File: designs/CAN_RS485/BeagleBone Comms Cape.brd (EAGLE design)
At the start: 71.8 x 58.4 mm, 59 parts, among them T1 PBSS4350Z 50V 3A, T2 PBSS4350Z 50V 3A, T3 PBSS4350Z 50V 3A, T4 PBSS4350Z 50V 3A, T5 PBSS4350Z 50V 3A, T6 PBSS4350Z 50V 3A, T7 PBSS4350Z 50V 3A, T8 PBSS4350Z 50V 3A

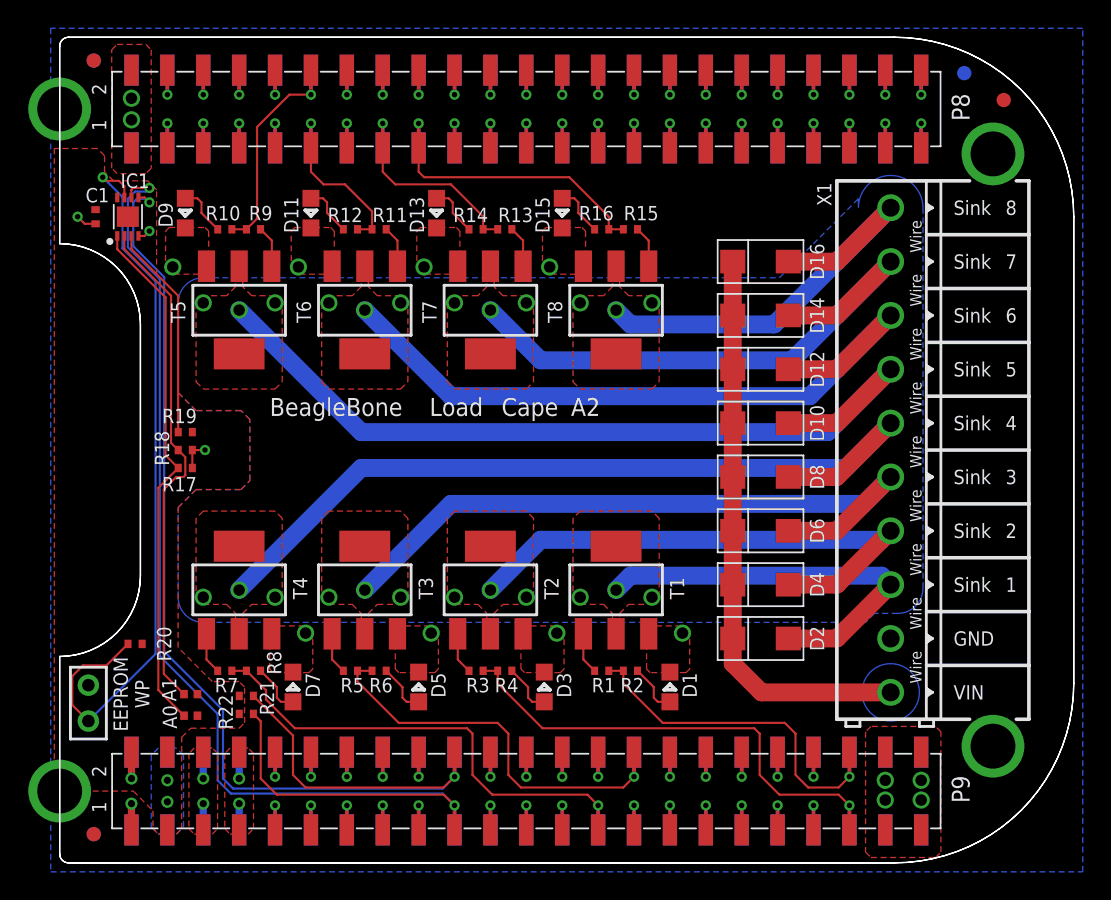
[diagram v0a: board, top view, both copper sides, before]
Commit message: Added the revised EAGLE schematics. Also removed two files that were probably not intended to be added as they are lock files in EAGLE.
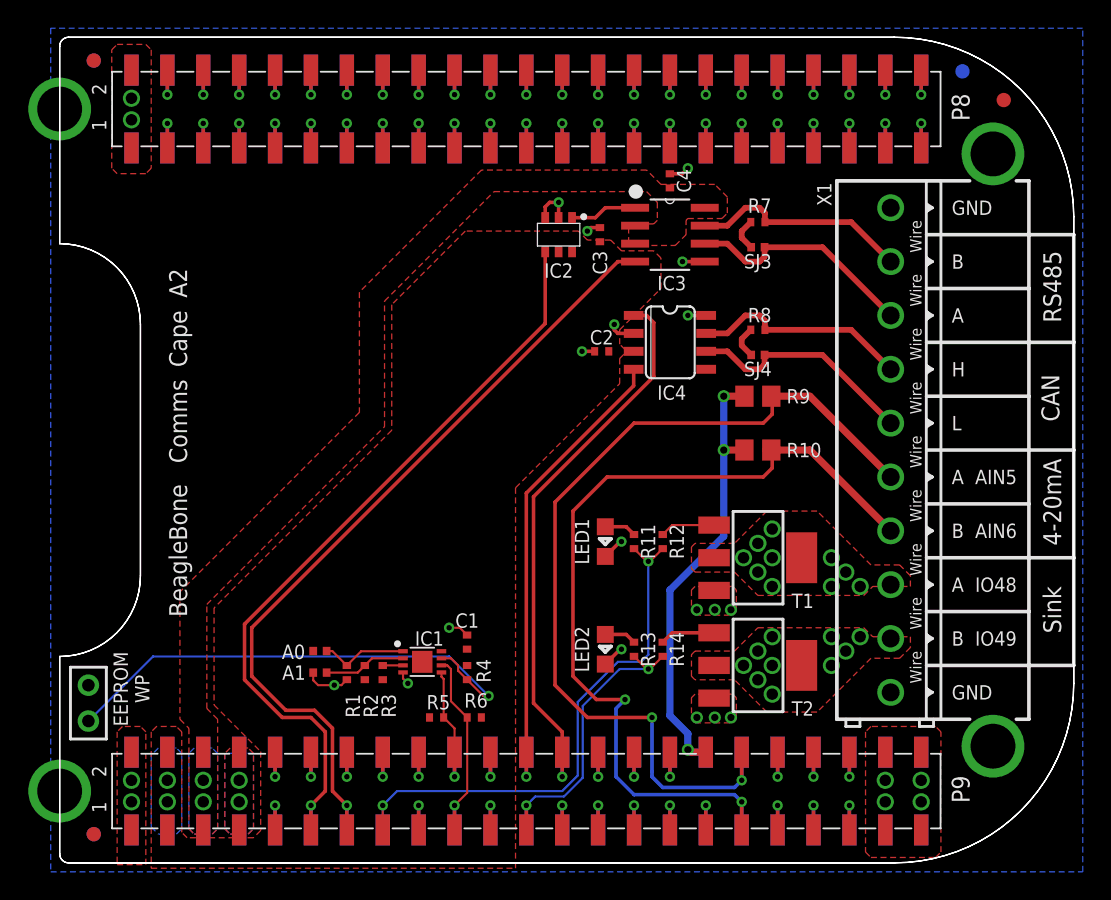
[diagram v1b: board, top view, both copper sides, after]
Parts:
- removed D1, D11, D13, D15, D3, D5, D7, D9: RED, GHI-BasicComponents:0805-LED
- removed D10, D12, D14, D16, D2, D4, D6, D8: STPS140A, GHI:DIODE_SMA
- removed R15: 330, GHI-BasicComponents:0402
- removed R16, R17, R18, R19, R20: 1k, GHI-BasicComponents:0402
- removed R21, R22: DNP(2.2k), GHI-BasicComponents:0402
- removed T3, T4, T5, T6, T7, T8: PBSS4350Z 50V 3A, GHI-Transistors:SOT223
- added C2, C3, C4: .1uF, GHI-BasicComponents:0402
- added IC2: 74LVC1G57, GHI2:SOT-23-6
- added IC3: MAX13487EESA, GHI3:SOIC8
- added IC4: SN65HVD230, GHI:SO8
- added LED1, LED2: (no value), GHI-BasicComponents:0805-LED
- added SJ3, SJ4: (no value), GHI-Miscellaneous:SOLDER.JOINT(0402)
- C1: value (none) -> .1uF
- R1, R11, R13, R3: value 330 -> 1k
- R10: value 1k -> 75 .125W; device GHI-BasicComponents:0402 -> GHI-BasicComponents:0805
- R12, R14: value 1k -> 330
- R5: value 330 -> DNP(2.2k)
- R6: value 1k -> DNP(2.2k)
- R7: value 330 -> 120
- R8: value 1k -> 120
- R9: value 330 -> 75 .125W; device GHI-BasicComponents:0402 -> GHI-BasicComponents:0805
- moved R7 49.3 mm to (49.4, 45.3), turned to 0 degrees
- moved R8 43.1 mm to (49.4, 37.7)
- moved R10 40.8 mm to (49.4, 29.2), turned to 0 degrees
- moved C1 40.0 mm to (28.8, 15.6), turned to 90 degrees
- moved IC1 37.8 mm to (25.7, 14.2), turned to 90 degrees
- moved R9 37.6 mm to (49.4, 33.0)
- moved R14 32.5 mm to (42.7, 15.1), turned to 90 degrees
- moved R12 31.3 mm to (42.7, 22.7), turned to 90 degrees
- moved R13 31.1 mm to (40.6, 15.1), turned to 90 degrees
- moved R11 28.5 mm to (40.6, 22.7), turned to 90 degrees
- moved T2 19.7 mm to (49.4, 14.0), turned to 270 degrees
- moved R2 18.8 mm to (21.6, 13.5), turned to 90 degrees
- moved R1 18.0 mm to (20.3, 13.5), turned to 90 degrees
- moved T1 10.3 mm to (49.4, 21.6), turned to 270 degrees
- moved SJ1 10.2 mm to (18.4, 15.0), turned to 0 degrees
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- renumbered BB.CAPE1 to BB.CAPE2
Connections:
- removed net N$10: R7.2, T4.1
- removed net N$11: D5.A, R6.2
- removed net N$12: R5.2, T3.1
- removed net N$13: D3.A, R4.2
- removed net N$3: D13.A, R14.2
- removed net N$35: R3.2, T2.1
- removed net N$36: D1.A, R2.2
- removed net N$37: R1.2, T1.1
- removed net N$38: D15.A, R16.2
- removed net N$39: R15.2, T8.1
- removed net N$6: R11.2, T6.1
- removed net N$9: D7.A, R8.2
- removed net P9.11: BB.CAPE2.B9.11, BB.CAPE2.T9.11
- removed net P9.13: BB.CAPE2.B9.13, BB.CAPE2.T9.13
- removed net P9.15: BB.CAPE2.B9.15, BB.CAPE2.T9.15
- removed net P9.23: BB.CAPE2.B9.23, BB.CAPE2.T9.23
- removed net P9.24: BB.CAPE2.B9.24, BB.CAPE2.T9.24
- removed net P9.26: BB.CAPE2.B9.26, BB.CAPE2.T9.26
- removed net P9.34: BB.CAPE2.B9.34, BB.CAPE2.T9.34
- removed net P9.35: BB.CAPE2.B9.35, BB.CAPE2.T9.35
- removed net P9.36: BB.CAPE2.B9.36, BB.CAPE2.T9.36
- removed net SINK1: BB.CAPE2.B9.42, BB.CAPE2.T9.42, R1.1, R2.1
- removed net SINK1.TB: D2.A, T1.2, T1.4, X1.8
- removed net SINK2: BB.CAPE2.B9.41, BB.CAPE2.T9.41, R3.1, R4.1
- removed net SINK2.TB: D4.A, T2.2, T2.4, X1.7
- removed net SINK3: BB.CAPE2.B9.30, BB.CAPE2.T9.30, R5.1, R6.1
- removed net SINK3.TB: D6.A, T3.2, T3.4, X1.6
- removed net SINK4: BB.CAPE2.B9.27, BB.CAPE2.T9.27, R7.1, R8.1
- removed net SINK4.TB: D8.A, T4.2, T4.4, X1.5
- removed net SINK5: BB.CAPE2.B8.12, BB.CAPE2.T8.12, R10.1, R9.1
- removed net SINK5.TB: D10.A, T5.2, T5.4, X1.4
- removed net SINK6: BB.CAPE2.B8.11, BB.CAPE2.T8.11, R11.1, R12.1
- removed net SINK6.TB: D12.A, T6.2, T6.4, X1.3
- removed net SINK7: BB.CAPE2.B8.15, BB.CAPE2.T8.15, R13.1, R14.1
- removed net SINK7.TB: D14.A, T7.2, T7.4, X1.2
- removed net SINK8: BB.CAPE2.B8.17, BB.CAPE2.T8.17, R15.1, R16.1
- removed net SINK8.TB: D16.A, T8.2, T8.4, X1.1
- removed net VDD_5V: BB.CAPE2.B9.5, BB.CAPE2.B9.6, BB.CAPE2.T9.5, BB.CAPE2.T9.6
- removed net VIN: D10.K, D12.K, D14.K, D16.K, D2.K, D4.K, D6.K, D8.K, X1.10
- new net 4-20MA.LOOP.A: BB.CAPE2.B9.36, BB.CAPE2.T9.36, R9.2, X1.6
- new net 4-20MA.LOOP.B: BB.CAPE2.B9.35, BB.CAPE2.T9.35, R10.2, X1.7
- new net AGND: BB.CAPE2.B9.34, BB.CAPE2.T9.34, R10.1, R9.1
- new net CAN.H: IC4.7, R8.2, X1.4
- new net CAN.L: IC4.6, SJ4.2, X1.5
- new net CAN.RD: BB.CAPE2.B9.24, BB.CAPE2.T9.24, IC4.4
- new net CAN.TD: BB.CAPE2.B9.26, BB.CAPE2.T9.26, IC4.1
- new net P8.11: BB.CAPE2.B8.11, BB.CAPE2.T8.11
- new net P8.12: BB.CAPE2.B8.12, BB.CAPE2.T8.12
- new net P8.15: BB.CAPE2.B8.15, BB.CAPE2.T8.15
- new net P8.17: BB.CAPE2.B8.17, BB.CAPE2.T8.17
- new net P9.27: BB.CAPE2.B9.27, BB.CAPE2.T9.27
- new net P9.30: BB.CAPE2.B9.30, BB.CAPE2.T9.30
- new net P9.41: BB.CAPE2.B9.41, BB.CAPE2.T9.41
- new net P9.42: BB.CAPE2.B9.42, BB.CAPE2.T9.42
- new net RS485.A: IC3.6, SJ3.2, X1.3
- new net RS485.B: IC3.7, R7.2, X1.2
- new net RS485.RX: BB.CAPE2.B9.11, BB.CAPE2.T9.11, IC2.Y
- new net RS485.RX.5V: IC2.IN1, IC3.1
- new net RS485.TX: BB.CAPE2.B9.13, BB.CAPE2.T9.13, IC3.4
- new net SINK.A: BB.CAPE2.B9.15, BB.CAPE2.T9.15, R11.1, R12.1
- new net SINK.A-BASE: R12.2, T1.1
- new net SINK.A-TB: T1.2, T1.4, X1.8
- new net SINK.B: BB.CAPE2.B9.23, BB.CAPE2.T9.23, R13.1, R14.1
- new net SINK.B-BASE: R14.2, T2.1
- new net SINK.B-TB: T2.2, T2.4, X1.9
- new net SYS.VOUT: BB.CAPE2.B9.7, BB.CAPE2.B9.8, BB.CAPE2.T9.7, BB.CAPE2.T9.8
- net +5V: now also BB.CAPE2.B9.5, BB.CAPE2.B9.6, BB.CAPE2.T9.5, BB.CAPE2.T9.6, C4.1, IC3.2, IC3.3, IC3.8; no longer BB.CAPE2.B9.7, BB.CAPE2.B9.8, BB.CAPE2.T9.7, BB.CAPE2.T9.8
- net A0: now also R1.2; no longer R17.2
- net A1: now also R2.2; no longer R18.2
- net A2: now also R3.2; no longer R19.2
- net GND: now also C2.2, C3.2, C4.2, IC2.GND, IC2.IN0, IC3.5, IC4.2, IC4.8, LED1.K, LED2.K, R1.1, SJ2.1, X1.1, X1.10; no longer D1.K, D11.K, D13.K, D15.K, D3.K, D5.K, D7.K, D9.K, R17.1, R18.1, T3.3, T4.3, T5.3, T6.3, T7.3, T8.3, X1.9
- net N$4: now also R8.1, SJ4.1; no longer R13.2, T7.1
- net N$5: now also R7.1, SJ3.1; no longer D11.A, R12.2
- net N$7: now also LED1.A, R11.2; no longer D9.A, R10.2
- net N$8: now also LED2.A, R13.2; no longer R9.2, T5.1
- net SCL: now also R6.1; no longer R22.1
- net SDA: now also R5.1; no longer R21.1
- net VCC: now also C2.1, C3.1, IC2.IN2, IC2.VCC, IC4.3, R2.1, R3.1, R4.2, R5.2, R6.2; no longer R19.1, R20.2, R21.2, R22.2, SJ2.1
- net WP: now also R4.1; no longer R20.1
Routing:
- net SDA: track 85.0 -> 9.50 mm, vias 2 -> 1
- net SCL: track 87.7 -> 14.7 mm, vias 2 -> 1
- net 4-20MA.LOOP.A: track 0.00 -> 65.8 mm, vias 0 -> 2
- net 4-20MA.LOOP.B: track 0.00 -> 62.8 mm, vias 0 -> 2
- net SINK5.TB: track 60.3 -> 0.00 mm, vias 3 -> 0
- net SINK4.TB: track 59.8 -> 0.00 mm, vias 3 -> 0
- net RS485.TX: track 0.00 -> 57.9 mm, vias 0 -> 1
- net RS485.RX: track 0.00 -> 55.4 mm, vias 0 -> 1
- net SINK6.TB: track 50.9 -> 0.00 mm, vias 3 -> 0
- net SINK3.TB: track 49.3 -> 0.00 mm, vias 3 -> 0
- net SINK7.TB: track 41.5 -> 0.00 mm, vias 3 -> 0
- net VIN: track 40.5 -> 0.00 mm
- net CAN.TD: track 0.00 -> 39.9 mm, vias 0 -> 1
- net SINK.A: track 0.00 -> 39.1 mm, vias 0 -> 2
- net SINK2.TB: track 38.9 -> 0.00 mm, vias 3 -> 0
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- added copper zone on layer 16, net +5V
- added copper zone on layer 1, net SINK.A-TB
- added copper zone on layer 1, net SINK.B-TB
- added copper zone on layer 1, net SYS.VOUT
- added copper zone on layer 16, net SYS.VOUT
- removed copper zone on layer 16, net N$40
- removed copper zone on layer 16, net N$41
- removed copper zone on layer 1, net SINK1.TB
- removed copper zone on layer 1, net SINK2.TB
- removed copper zone on layer 1, net SINK3.TB
- removed copper zone on layer 1, net SINK4.TB
- removed copper zone on layer 1, net SINK5.TB
- removed copper zone on layer 1, net SINK6.TB
- removed copper zone on layer 1, net SINK7.TB
- removed copper zone on layer 1, net SINK8.TB
- removed copper zone on layer 1, net VDD_5V
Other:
- board text added: "4-20mA"
- board text added: "A"
- board text added: "AIN5"
- board text added: "AIN6"
- board text added: "B"
- board text added: "CAN"
- board text added: "Comms"
- board text added: "H"
- board text added: "IO48"
- board text added: "IO49"
- board text added: "L"
- board text added: "RS485"
- board text removed: "1"
- board text removed: "2"
- board text removed: "3"
- board text removed: "4"
- board text removed: "5"
- board text removed: "6"
- board text removed: "7"
- board text removed: "8"
- board text removed: "Load"
- board text removed: "VIN"
